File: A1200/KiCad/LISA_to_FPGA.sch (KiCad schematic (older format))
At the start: 17 parts, among them J1 Conn_01x04, J2 Conn_01x40, U1 LM1117-3.3, U2 74LVC16244ADGG, U3 74LVC16244ADGG, U4 LISA

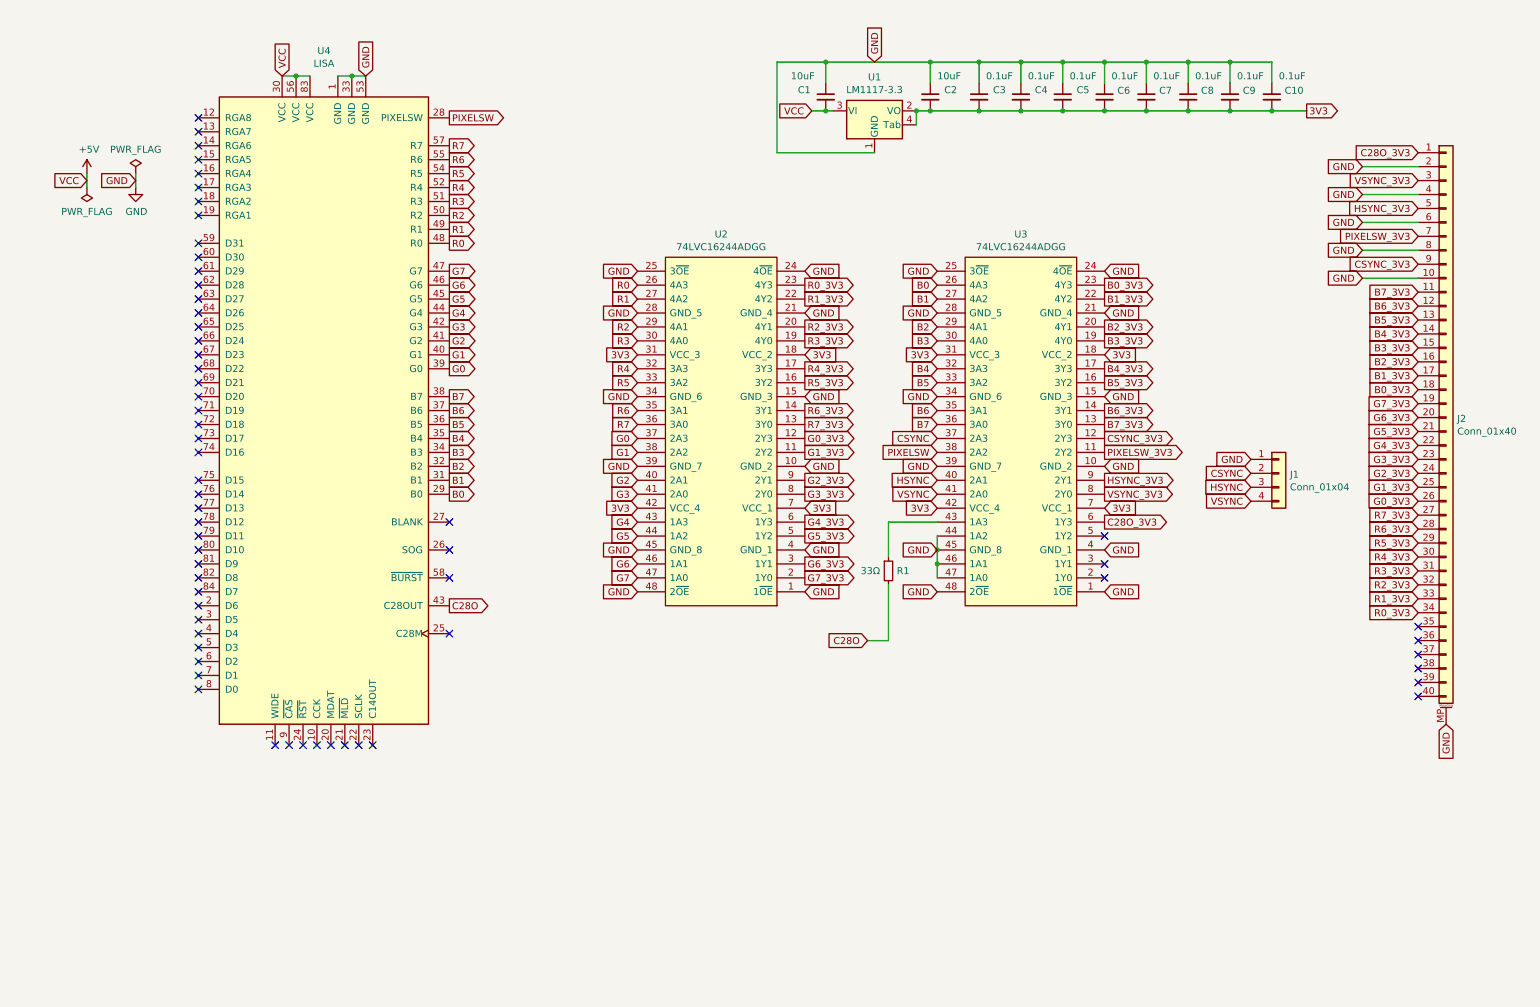
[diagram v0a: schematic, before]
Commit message: Add a RP2354B to the design
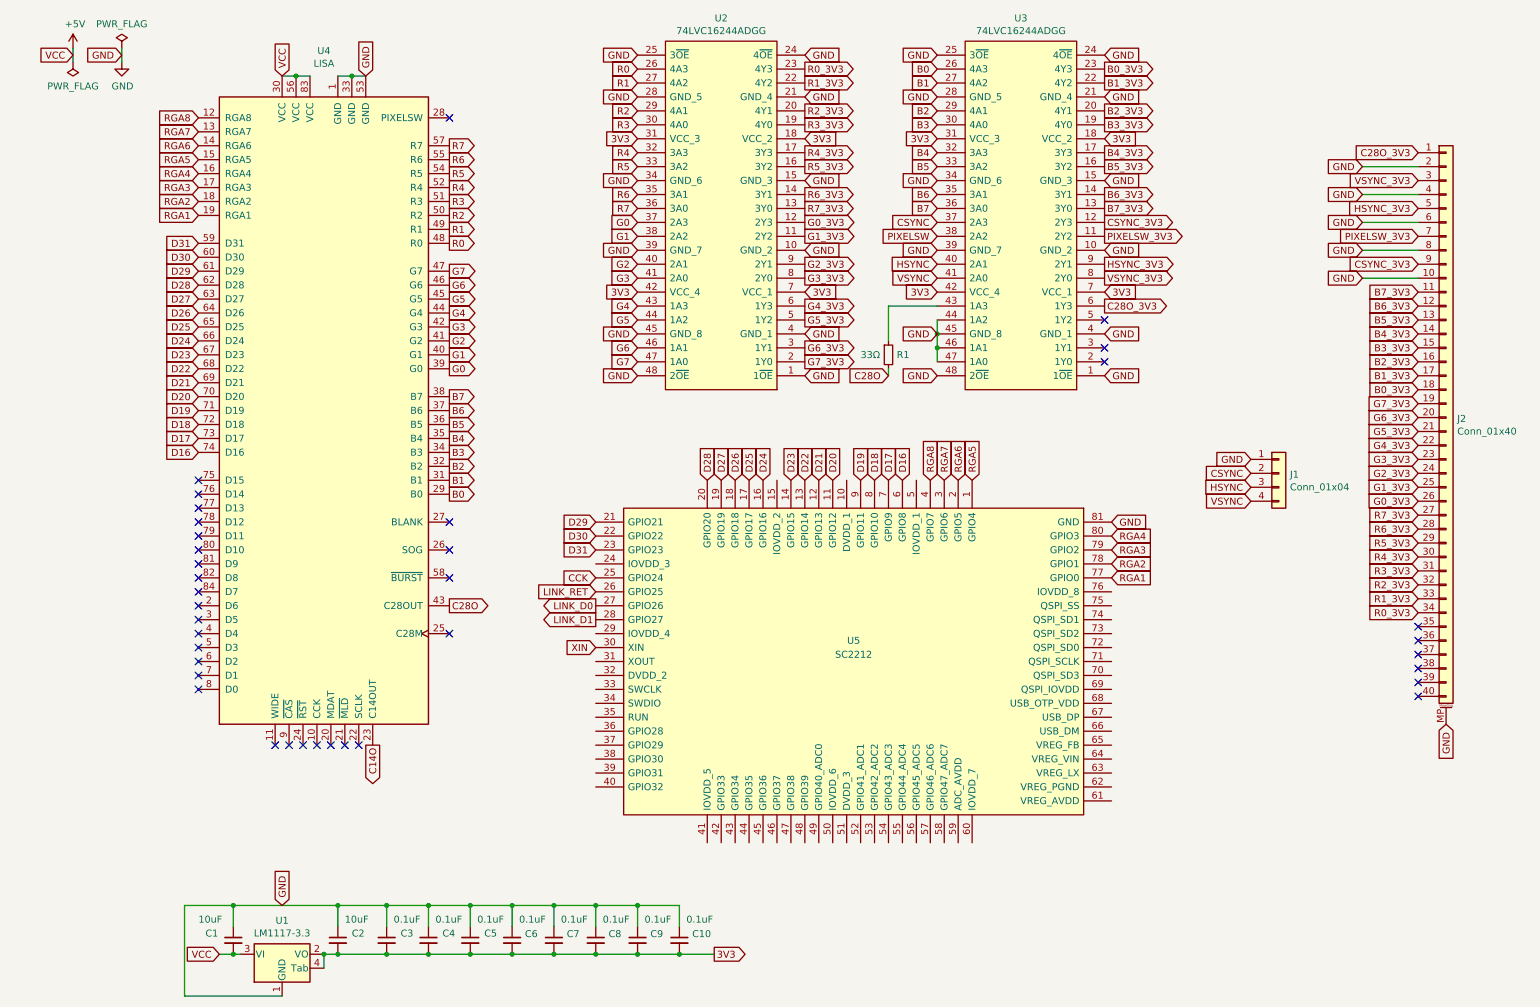
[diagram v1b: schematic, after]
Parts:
- added U5: SC2212, LISA_to_FPGA:QFN40P1000X1000X90-81N-D, symbol LISA_to_FPGA:SC2212
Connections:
- net GND: now also U5.81 (GND)
- net PIXELSW: no longer U4.28 (PIXELSW)
- net RGA8: now reaches U4.12 (RGA8)
- net RGA8: now also U5.4 (GPIO7)
- net RGA7: now reaches U4.13 (RGA7)
- net RGA7: now also U5.3 (GPIO6)
- net RGA6: now reaches U4.14 (RGA6)
- net RGA6: now also U5.2 (GPIO5)
- net RGA5: now reaches U4.15 (RGA5)
- net RGA5: now also U5.1 (GPIO4)
- net RGA4: now reaches U4.16 (RGA4)
- net RGA4: now also U5.80 (GPIO3)
- net RGA3: now reaches U4.17 (RGA3)
- net RGA3: now also U5.79 (GPIO2)
- net RGA2: now reaches U4.18 (RGA2)
- net RGA2: now also U5.78 (GPIO1)
- net RGA1: now reaches U4.19 (RGA1)
- net RGA1: now also U5.77 (GPIO0)
- net C14O: now reaches U4.23 (C14OUT)
- net D31: now reaches U4.59 (D31)
- net D31: now also U5.23 (GPIO23)
- net D30: now reaches U4.60 (D30)
- net D30: now also U5.22 (GPIO22)
- net D29: now reaches U4.61 (D29)
- net D29: now also U5.21 (GPIO21)
- net D28: now reaches U4.62 (D28)
- net D28: now also U5.20 (GPIO20)
- net D27: now reaches U4.63 (D27)
- net D27: now also U5.19 (GPIO19)
- net D26: now reaches U4.64 (D26)
- net D26: now also U5.18 (GPIO18)
- net D25: now reaches U4.65 (D25)
- net D25: now also U5.17 (GPIO17)
- net D24: now reaches U4.66 (D24)
- net D24: now also U5.16 (GPIO16)
- net D23: now reaches U4.67 (D23)
- net D23: now also U5.14 (GPIO15)
- net D22: now reaches U4.68 (D22)
- net D22: now also U5.13 (GPIO14)
- net D21: now reaches U4.69 (D21)
- net D21: now also U5.12 (GPIO13)
- net D20: now reaches U4.70 (D20)
- net D20: now also U5.11 (GPIO12)
- net D19: now reaches U4.71 (D19)
- net D19: now also U5.9 (GPIO11)
- net D18: now reaches U4.72 (D18)
- net D18: now also U5.8 (GPIO10)
- net D17: now reaches U4.73 (D17)
- net D17: now also U5.7 (GPIO9)
- net D16: now reaches U4.74 (D16)
- net D16: now also U5.6 (GPIO8)
- new net CCK: U5.25 (GPIO24)
- new net LINK_D0: U5.27 (GPIO26)
- new net LINK_D1: U5.28 (GPIO27)
- new net LINK_RET: U5.26 (GPIO25)
- new net XIN: U5.30 (XIN)
- no-connect marks 61 -> 37
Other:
- moved on the sheet: C1, C10, C2, C3, C4, C5, C6, C7, C8, C9, R1, U1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

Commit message: Change single resistors to 0603, add 330 OHm resistor packs, change U2,U3 to 74LVC162244ADGG with built-in 30 ohm termination resistors, fix to handsolder footprint for RP2354B, pin assignment and more routing
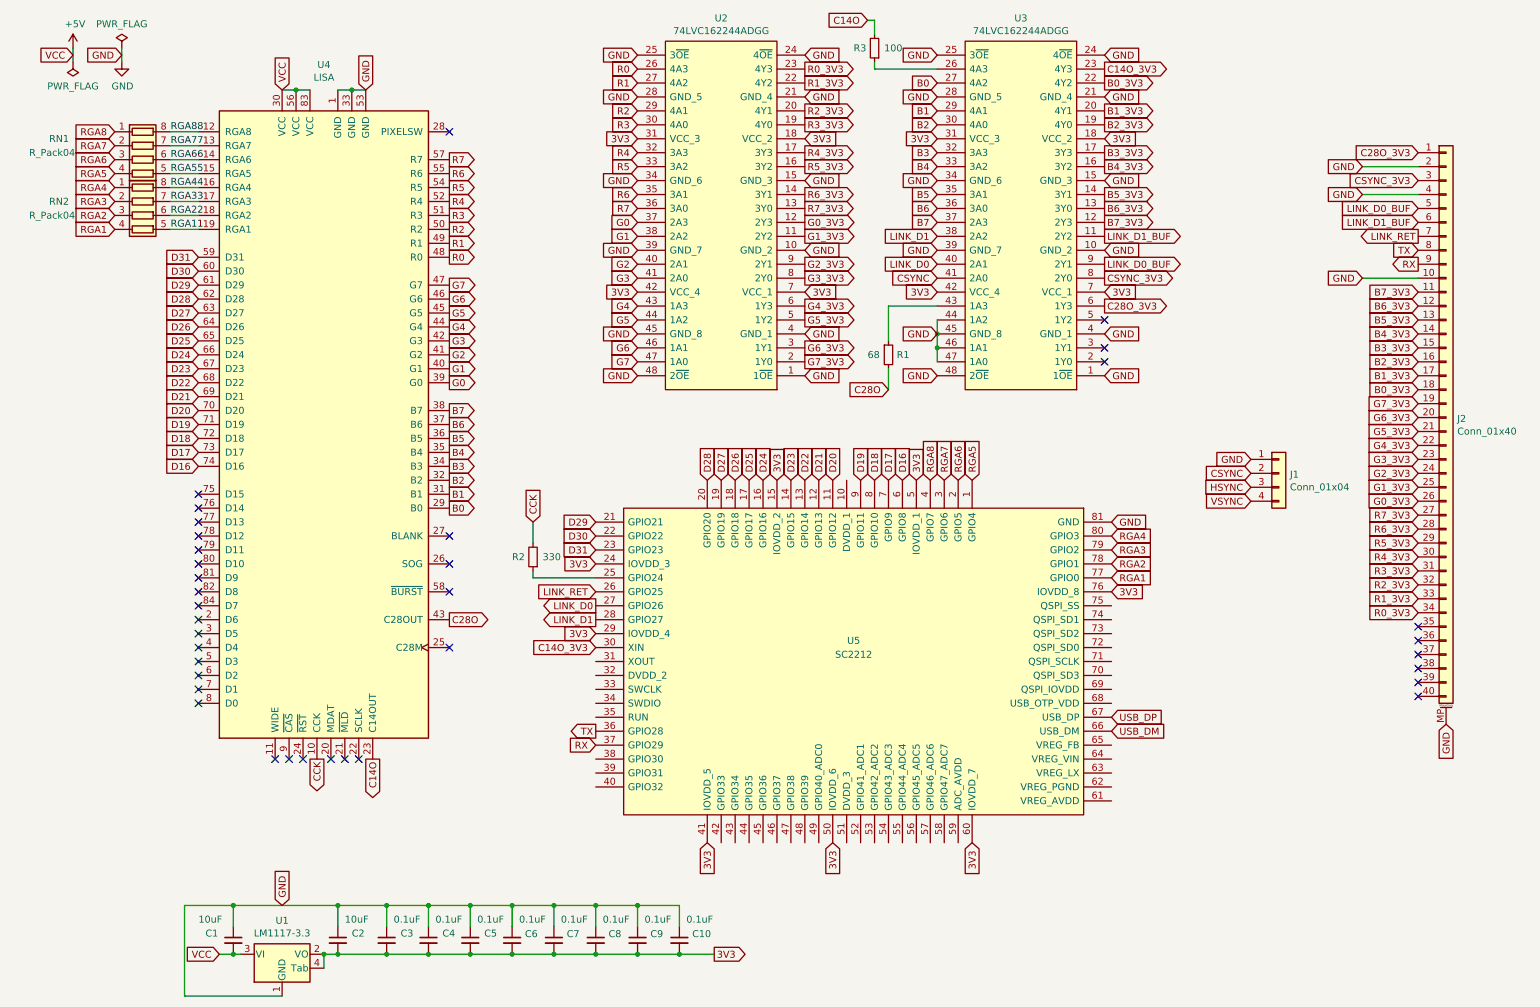
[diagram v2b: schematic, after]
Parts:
- added R2: 330, Resistor_SMD:R_0603_1608Metric_Pad0.98x0.95mm_HandSolder, symbol Device:R_Small
- added R3: 100, Resistor_SMD:R_0603_1608Metric_Pad0.98x0.95mm_HandSolder, symbol Device:R_Small
- added RN1, RN2: R_Pack04, Resistor_SMD:R_Array_Convex_4x0603, symbol Device:R_Pack04
- R1: value 33Ω -> 68; footprint Resistor_SMD:R_0805_2012Metric_Pad1.20x1.40mm_HandSolder -> Resistor_SMD:R_0603_1608Metric_Pad0.98x0.95mm_HandSolder
- U2, U3: value 74LVC16244ADGG -> 74LVC162244ADGG
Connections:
- net PIXELSW is gone; now on net LINK_D1: U3.38 (2A2)
- net VSYNC_3V3 is gone; now on net CSYNC_3V3: J2.3 (Pin_3), U3.8 (2Y0)
- net 3V3: now also U5.15 (IOVDD_2), U5.24 (IOVDD_3), U5.29 (IOVDD_4), U5.41 (IOVDD_5), U5.5 (IOVDD_1), U5.50 (IOVDD_6), U5.60 (IOVDD_7), U5.76 (IOVDD_8)
- net B0: now also U3.27 (4A2); no longer U3.26 (4A3)
- net B0_3V3: now also U3.22 (4Y2); no longer U3.23 (4Y3)
- net B1: now also U3.29 (4A1); no longer U3.27 (4A2)
- net B1_3V3: now also U3.20 (4Y1); no longer U3.22 (4Y2)
- net B2: now also U3.30 (4A0); no longer U3.29 (4A1)
- net B2_3V3: now also U3.19 (4Y0); no longer U3.20 (4Y1)
- net B3: now also U3.32 (3A3); no longer U3.30 (4A0)
- net B3_3V3: now also U3.17 (3Y3); no longer U3.19 (4Y0)
- net B4: now also U3.33 (3A2); no longer U3.32 (3A3)
- net B4_3V3: now also U3.16 (3Y2); no longer U3.17 (3Y3)
- net B5: now also U3.35 (3A1); no longer U3.33 (3A2)
- net B5_3V3: now also U3.14 (3Y1); no longer U3.16 (3Y2)
- net B6: now also U3.36 (3A0); no longer U3.35 (3A1)
- net B6_3V3: now also U3.13 (3Y0); no longer U3.14 (3Y1)
- net B7: now also U3.37 (2A3); no longer U3.36 (3A0)
- net B7_3V3: now also U3.12 (2Y3); no longer U3.13 (3Y0)
- net C14O: now also R3.2
- net CCK: now also U4.10 (CCK), R2.2; no longer U5.25 (GPIO24)
- net CSYNC: now also U3.41 (2A0); no longer U3.37 (2A3)
- net CSYNC_3V3: no longer J2.9 (Pin_9), U3.12 (2Y3)
- net GND: no longer J2.6 (Pin_6), J2.8 (Pin_8)
- net HSYNC: no longer U3.40 (2A1)
- net LINK_D0: now also U3.40 (2A1)
- net LINK_RET: now also J2.7 (Pin_7)
- net RGA1: now also RN2.4 (R4.1); no longer U4.19 (RGA1)
- net RGA2: now also RN2.3 (R3.1); no longer U4.18 (RGA2)
- net RGA3: now also RN2.2 (R2.1); no longer U4.17 (RGA3)
- net RGA4: now also RN2.1 (R1.1); no longer U4.16 (RGA4)
- net RGA5: now also RN1.4 (R4.1); no longer U4.15 (RGA5)
- net RGA6: now also RN1.3 (R3.1); no longer U4.14 (RGA6)
- net RGA7: now also RN1.2 (R2.1); no longer U4.13 (RGA7)
- net RGA8: now also RN1.1 (R1.1); no longer U4.12 (RGA8)
- net VSYNC: no longer U3.41 (2A0)
- net TX: now reaches U5.36 (GPIO28)
- net TX: now also J2.8 (Pin_8)
- net RX: now reaches U5.37 (GPIO29)
- net RX: now also J2.9 (Pin_9)
- net USB_DM: now reaches U5.66 (USB_DM)
- net USB_DP: now reaches U5.67 (USB_DP)
- net HSYNC_3V3 renamed LINK_D0_BUF
- net PIXELSW_3V3 renamed LINK_D1_BUF
- net LINK_D1_BUF: now also J2.6 (Pin_6); no longer J2.7 (Pin_7)
- net XIN renamed C14O_3V3
- net C14O_3V3: now also U3.23 (4Y3)
- new net: R3.1, U3.26 (4A3)
- new net: R2.1, U5.25 (GPIO24)
- new net RGA11: RN2.5 (R4.2), U4.19 (RGA1)
- new net RGA22: RN2.6 (R3.2), U4.18 (RGA2)
- new net RGA33: RN2.7 (R2.2), U4.17 (RGA3)
- new net RGA44: RN2.8 (R1.2), U4.16 (RGA4)
- new net RGA55: RN1.5 (R4.2), U4.15 (RGA5)
- new net RGA66: RN1.6 (R3.2), U4.14 (RGA6)
- new net RGA77: RN1.7 (R2.2), U4.13 (RGA7)
- new net RGA88: RN1.8 (R1.2), U4.12 (RGA8)
- no-connect marks 37 -> 36
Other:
- moved on the sheet: U4

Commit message: Add power circuit for 1.1V
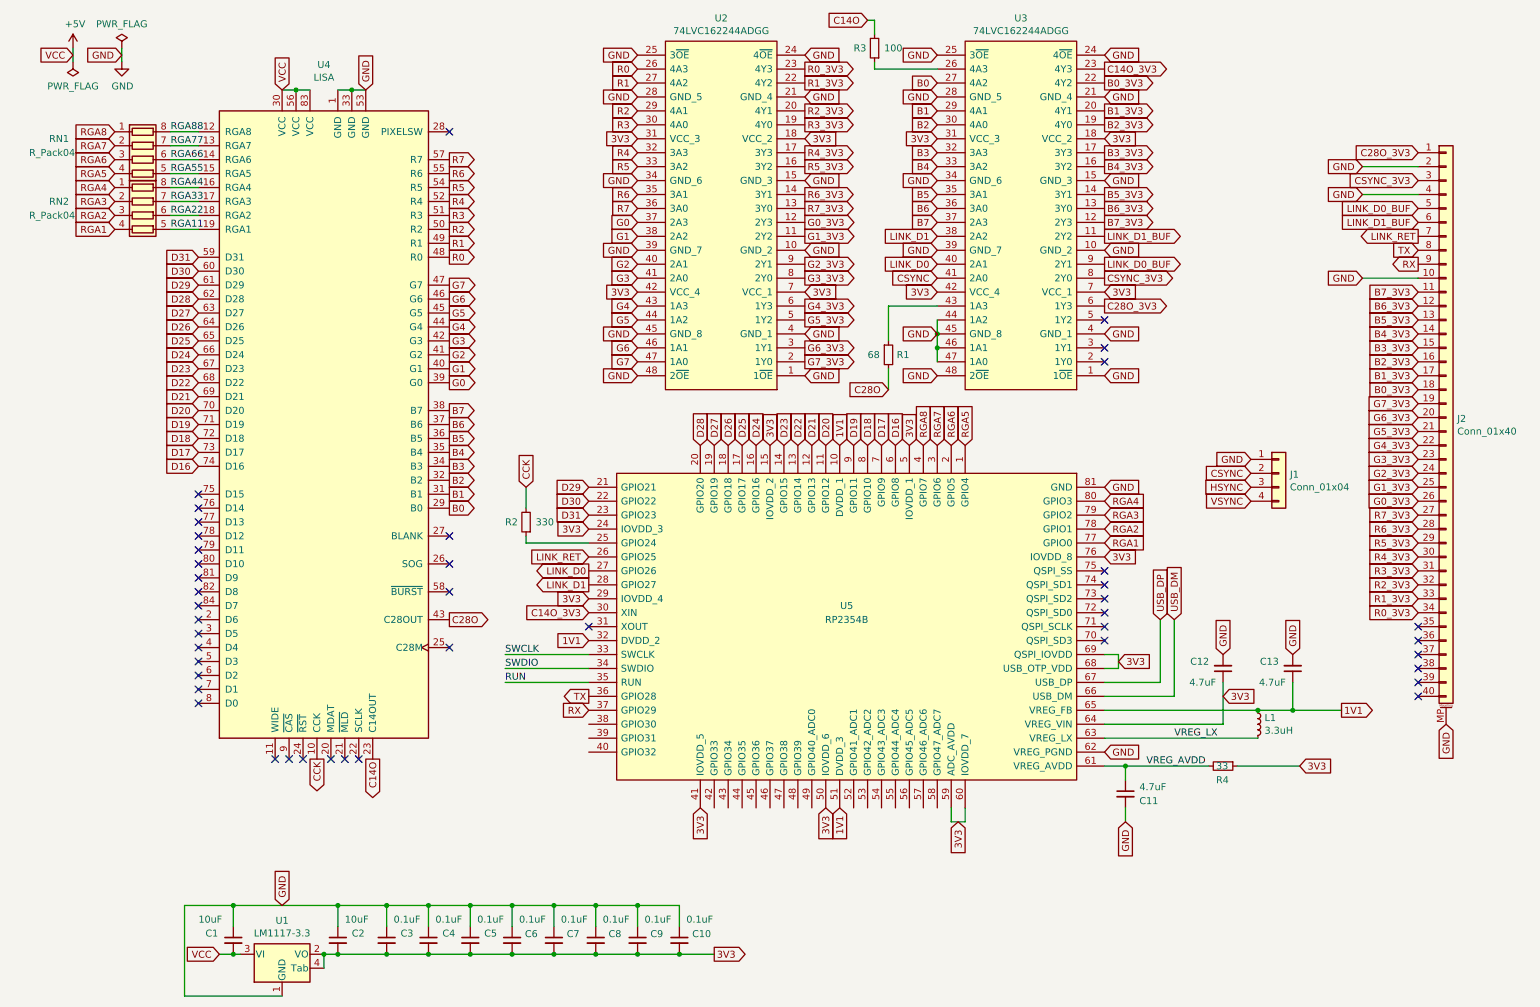
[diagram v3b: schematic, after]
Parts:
- added C11, C12, C13: 4.7uF, Capacitor_SMD:C_0805_2012Metric_Pad1.18x1.45mm_HandSolder, symbol Device:C_Small
- added L1: 3.3uH, LISA_to_FPGA:AOTAB201610S3R3101T, symbol Device:L_Small
- added R4: 33, Resistor_SMD:R_0603_1608Metric_Pad0.98x0.95mm_HandSolder, symbol Device:R_Small
- U5: value SC2212 -> RP2354B
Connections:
- net 3V3: now also U5.59 (ADC_AVDD), U5.64 (VREG_VIN), U5.68 (USB_OTP_VDD), U5.69 (QSPI_IOVDD), C12.1, R4.1
- net GND: now also U5.62 (VREG_PGND), C11.2, C12.2, C13.2
- net 1V1: now reaches U5.10 (DVDD_1)
- net 1V1: now also U5.32 (DVDD_2), U5.51 (DVDD_3), U5.65 (VREG_FB), C13.1, L1.1
- net SWCLK: now reaches U5.33 (SWCLK)
- net SWDIO: now reaches U5.34 (SWDIO)
- net RUN: now reaches U5.35 (RUN)
- net VREG_AVDD: now reaches U5.61 (VREG_AVDD)
- net VREG_AVDD: now also C11.1, R4.2
- net VREG_LX: now reaches U5.63 (VREG_LX)
- net VREG_LX: now also L1.2
- no-connect marks 36 -> 43
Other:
- moved on the sheet: R2, U5
